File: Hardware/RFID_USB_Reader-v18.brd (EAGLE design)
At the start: 50.8 x 30.5 mm, 38 parts, among them Q1 MMBT2222, U1 ID-12/20SMD, U5 CH340C

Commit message: post checklist changes
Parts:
- added FRAME1: FRAME-LETTER, SparkFun-Aesthetics:CREATIVE_COMMONS
- added JP1, JP5: FIDUCIAL1X2, SparkFun:FIDUCIAL-1X2
- added LOGO4: REVISION, SparkFun-Aesthetics:REVISION
- added U$18: (no value), buzzard_labels (13):USB_RFID_READER0
- LED1: value GREEN -> BLUE
- U$17: device buzzard_labels (12):PWR0 -> buzzard_labels (13):USB_RFID_READER0
- U$2: value CREATIVE_COMMONS -> (none); device SparkFun:CREATIVE_COMMONS -> buzzard_labels (11):BZR3
- moved U$17 26.0 mm to (25.1, 12.7)
- moved U$2 15.1 mm to (0.25, 5.91)
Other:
- board text added: "A. England"
- board text added: "A. Weiss"
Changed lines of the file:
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@@
 <wire x1="0" y1="30.48" x2="0" y2="0" width="0.2032" layer="20"/>
 <text x="8.89" y="0.4445" size="1.27" layer="16" font="vector" ratio="15" rot="MR0">v13</text>
+<dimension x1="50.8" y1="30.48" x2="0" y2="30.48" x3="25.4" y3="36.83" textsize="1.778" layer="47" unit="inch"/>
+<dimension x1="0" y1="30.48" x2="0" y2="0" x3="-5.08" y3="15.24" textsize="1.778" layer="47" unit="inch"/>
+<dimension x1="2.54" y1="27.94" x2="48.26" y2="27.94" x3="25.4" y3="33.02" textsize="1.778" layer="47" unit="inch"/>
+<dimension x1="2.54" y1="27.94" x2="2.54" y2="2.54" x3="-1.27" y3="15.24" textsize="1.778" layer="47" unit="inch"/>
+<text x="26.67" y="-12.7" size="1.778" layer="51" font="vector">A. Weiss</text>
+<text x="26.67" y="-15.24" size="1.778" layer="51" font="vector">A. England</text>
 </plain>
 <attributes>
@@
 </autorouter>
 <elements>
-<element name="LED1" library="SparkFun-LED" package="LED-0603" value="GREEN" x="2.54" y="6.985" smashed="yes">
+<element name="LED1" library="SparkFun-LED" package="LED-0603" value="BLUE" x="2.54" y="6.985" smashed="yes">
 <attribute name="NAME" x="1.8415" y="6.096" size="0.4064" layer="25" rot="R90"/>
-<attribute name="PROD_ID" value="DIO-00821" x="2.54" y="6.985" size="1.778" layer="27" display="off"/>
-<attribute name="VALUE" value="GREEN" x="1.5875" y="6.477" size="0.4064" layer="27" rot="R90"/>
+<attribute name="PROD_ID" value="DIO-08575" x="2.54" y="6.985" size="1.778" layer="27" display="off"/>
+<attribute name="VALUE" value="BLUE" x="1.5875" y="6.477" size="0.4064" layer="27" rot="R90"/>
 </element>
 <element name="R1" library="SparkFun-Resistors" package="0603" value="330" x="5.08" y="7.9375" smashed="yes" rot="R270">
@@
 <attribute name="VALUE" x="10.795" y="10.922" size="0.6096" layer="27" ratio="10"/>
 </element>
-<element name="U$2" library="SparkFun" package="CREATIVE_COMMONS" value="CREATIVE_COMMONS" x="-2.54" y="-8.89"/>
 <element name="BUZZ" library="SparkFun-Jumpers" package="SMT-JUMPER_2_NO_NO-SILK" package3d_urn="urn:adsk.eagle:package:39277/1" value="buzz" x="12.7" y="6.35" rot="MR180"/>
 <element name="JP2" library="SparkFun" package="FIDUCIAL-1X2" value="FIDUCIAL1X2" x="6.35" y="5.08"/>
@@
 <element name="U$15" library="buzzard_labels (11)" package="TXR1" value="" x="49.2125" y="12.7" rot="MR0"/>
 <element name="U$16" library="buzzard_labels (11)" package="CP2" value="" x="49.2125" y="10.16" rot="MR0"/>
-<element name="U$17" library="buzzard_labels (12)" package="PWR0" value="" x="0.0635" y="5.588"/>
 <element name="LOGO1" library="SparkFun-Aesthetics" package="SFE_LOGO_NAME_FLAME_.1" value="SFE_LOGO_NAME_FLAME.1_INCH" x="31.75" y="15.24"/>
 <element name="LOGO2" library="SparkFun-Aesthetics" package="SFE_LOGO_NAME_FLAME_.1" value="SFE_LOGO_NAME_FLAME.1_INCH" x="22.86" y="15.24" rot="MR0"/>
 <element name="LOGO3" library="SparkFun-Aesthetics" package="OSHW-LOGO-S" value="OSHW-LOGOS" x="48.26" y="6.35" rot="MR0"/>
+<element name="FRAME1" library="SparkFun-Aesthetics" package="CREATIVE_COMMONS" value="FRAME-LETTER" x="-3.282121875" y="-12.7">
+<attribute name="DESIGNER" value="" x="-3.282121875" y="-12.7" size="1.778" layer="27" display="off"/>
+<attribute name="REV" value="" x="-3.282121875" y="-12.7" size="1.778" layer="27" display="off"/>
+</element>
+<element name="LOGO4" library="SparkFun-Aesthetics" package="REVISION" value="REVISION" x="8.89" y="-15.24"/>
+<element name="JP1" library="SparkFun" package="FIDUCIAL-1X2" value="FIDUCIAL1X2" x="39.37" y="26.67" rot="MR0"/>
+<element name="JP5" library="SparkFun" package="FIDUCIAL-1X2" value="FIDUCIAL1X2" x="6.35" y="5.08" rot="MR0"/>
+<element name="U$2" library="buzzard_labels (11)" package="BZR3" value="" x="0.254" y="5.9055"/>
+<element name="U$17" library="buzzard_labels (13)" package="USB_RFID_READER0" value="" x="25.0825" y="12.7"/>
+<element name="U$18" library="buzzard_labels (13)" package="USB_RFID_READER0" value="" x="29.591" y="12.7" rot="MR0"/>
 </elements>
 <signals>

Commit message: post review changes
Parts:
- removed J2: (no value), SparkFun-Connectors:1X05_NO_SILK
- removed U$2: (no value), buzzard_labels (11):BZR3
- added J1: (no value), SparkFun-Connectors:1X07
- added U$19: (no value), buzzard_labels (14):ANT11
- added U$20: (no value), buzzard_labels (14):ANT13
- added U$21: (no value), buzzard_labels (14):ANT22
- added U$22: (no value), buzzard_labels (15):ANT24
- added U$23: (no value), buzzard_labels (15):IND0
- moved U$10 2.54 mm to (44.4, 15.2)
- moved U$14 2.54 mm to (49.1, 17.8)
- moved U$15 2.54 mm to (49.2, 15.2)
- moved U$9 2.54 mm to (45.3, 17.8)
- moved U$1 2.54 mm to (45.5, 7.62)
- moved U$16 2.54 mm to (49.2, 7.62)
- moved U$11 2.54 mm to (44.4, 22.9)
- moved U$12 2.54 mm to (49.1, 22.9)
- moved U$13 2.54 mm to (49.1, 20.3)
- moved U$3 2.54 mm to (44.6, 20.3)
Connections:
- net LED renamed INDICATOR
- new net ANT1: J1.3, U1.3
- new net ANT2: J1.2, U1.4
- net CP: now also J1.1; no longer J2.1
- net GND: now also J1.6; no longer J2.4
- net TX-O: now also J1.5; no longer J2.3
- net TX-O-RS232: now also J1.4; no longer J2.2
- net VCC: now also J1.7; no longer J2.5
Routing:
- net ANT1: track 0.00 -> 23.6 mm, vias 0 -> 1
- net ANT2: track 0.00 -> 21.9 mm, vias 0 -> 1
- net TX-O-RS232: track 37.7 -> 35.1 mm
- net TX-O: track 59.5 -> 57.0 mm
- net N$4: track 6.81 -> 5.39 mm
- net VCC: track 122.1 -> 121.1 mm
- net CP: track 25.3 -> 24.5 mm
- net GND: vias 7 -> 8

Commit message: post QC checklist changes
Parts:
- moved LOGO3 6.35 mm to (43.2, 2.54)
- moved JP2 1.27 mm to (5.08, 5.08)
- moved JP5 1.27 mm to (5.08, 5.08)
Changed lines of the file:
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@@
 </element>
 <element name="BUZZ" library="SparkFun-Jumpers" package="SMT-JUMPER_2_NO_NO-SILK" package3d_urn="urn:adsk.eagle:package:39277/1" value="buzz" x="12.7" y="6.35" rot="MR180"/>
-<element name="JP2" library="SparkFun" package="FIDUCIAL-1X2" value="FIDUCIAL1X2" x="6.35" y="5.08"/>
+<element name="JP2" library="SparkFun" package="FIDUCIAL-1X2" value="FIDUCIAL1X2" x="5.08" y="5.08"/>
 <element name="JP3" library="SparkFun" package="FIDUCIAL-1X2" value="FIDUCIAL1X2" x="39.37" y="26.67"/>
 <element name="U5" library="SparkFun-IC-Comms" package="SO016" value="CH340C" x="12.7" y="20.32" rot="R270">
@@
 <element name="LOGO1" library="SparkFun-Aesthetics" package="SFE_LOGO_NAME_FLAME_.1" value="SFE_LOGO_NAME_FLAME.1_INCH" x="31.75" y="15.24"/>
 <element name="LOGO2" library="SparkFun-Aesthetics" package="SFE_LOGO_NAME_FLAME_.1" value="SFE_LOGO_NAME_FLAME.1_INCH" x="22.86" y="15.24" rot="MR0"/>
-<element name="LOGO3" library="SparkFun-Aesthetics" package="OSHW-LOGO-S" value="OSHW-LOGOS" x="48.26" y="6.35" rot="MR0"/>
+<element name="LOGO3" library="SparkFun-Aesthetics" package="OSHW-LOGO-S" value="OSHW-LOGOS" x="43.18" y="2.54" rot="MR0"/>
 <element name="FRAME1" library="SparkFun-Aesthetics" package="CREATIVE_COMMONS" value="FRAME-LETTER" x="-3.282121875" y="-12.7">
 <attribute name="DESIGNER" value="" x="-3.282121875" y="-12.7" size="1.778" layer="27" display="off"/>
@@
 <element name="LOGO4" library="SparkFun-Aesthetics" package="REVISION" value="REVISION" x="8.89" y="-15.24"/>
 <element name="JP1" library="SparkFun" package="FIDUCIAL-1X2" value="FIDUCIAL1X2" x="39.37" y="26.67" rot="MR0"/>
-<element name="JP5" library="SparkFun" package="FIDUCIAL-1X2" value="FIDUCIAL1X2" x="6.35" y="5.08" rot="MR0"/>
+<element name="JP5" library="SparkFun" package="FIDUCIAL-1X2" value="FIDUCIAL1X2" x="5.08" y="5.08" rot="MR0"/>
 <element name="U$17" library="buzzard_labels (13)" package="USB_RFID_READER0" value="" x="25.0825" y="12.7"/>
 <element name="U$18" library="buzzard_labels (13)" package="USB_RFID_READER0" value="" x="29.591" y="12.7" rot="MR0"/>

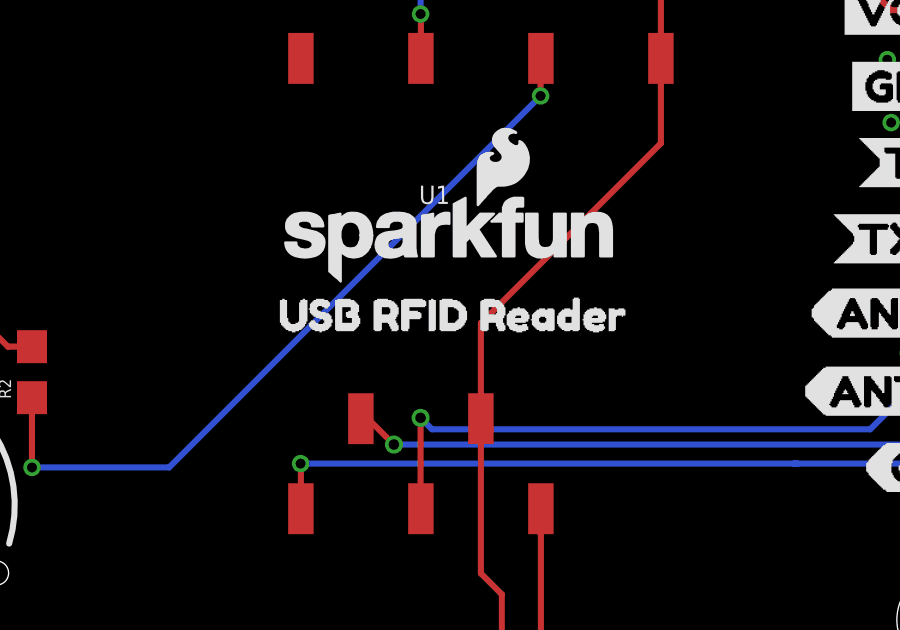
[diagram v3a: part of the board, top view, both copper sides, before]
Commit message: changing name to USB-C
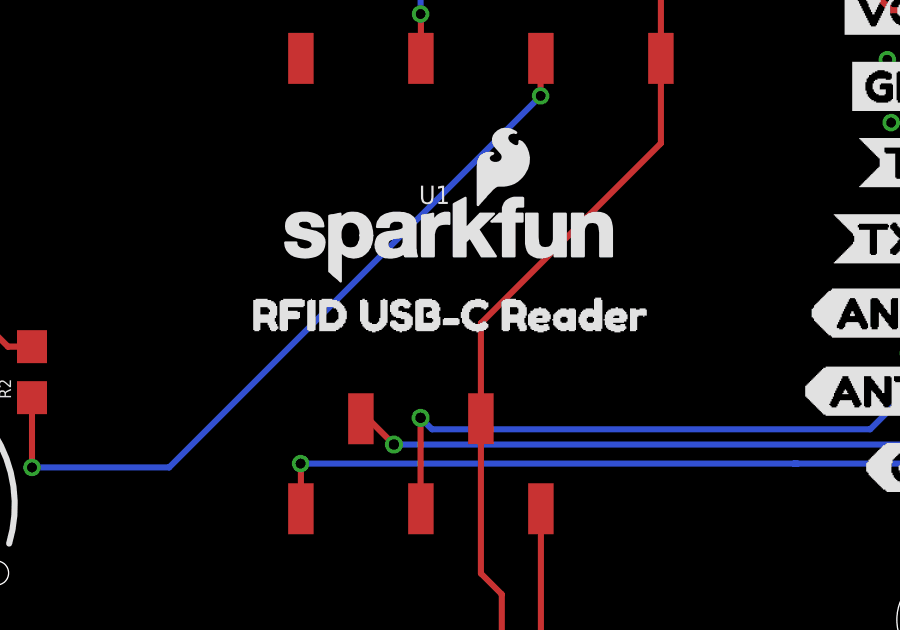
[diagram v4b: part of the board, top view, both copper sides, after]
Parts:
- U$17, U$18: device buzzard_labels (13):USB_RFID_READER0 -> buzzard_labels (16):RFID_USB#C_READER0
- moved U$17 0.89 mm to (24.2, 12.7)
- moved U$18 0.76 mm to (30.4, 12.7)
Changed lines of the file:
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@@
 <element name="JP1" library="SparkFun" package="FIDUCIAL-1X2" value="FIDUCIAL1X2" x="39.37" y="26.67" rot="MR0"/>
 <element name="JP5" library="SparkFun" package="FIDUCIAL-1X2" value="FIDUCIAL1X2" x="5.08" y="5.08" rot="MR0"/>
-<element name="U$17" library="buzzard_labels (13)" package="USB_RFID_READER0" value="" x="25.0825" y="12.7"/>
-<element name="U$18" library="buzzard_labels (13)" package="USB_RFID_READER0" value="" x="29.591" y="12.7" rot="MR0"/>
+<element name="U$17" library="buzzard_labels (16)" package="RFID_USB#C_READER0" value="" x="24.1935" y="12.7"/>
+<element name="U$18" library="buzzard_labels (16)" package="RFID_USB#C_READER0" value="" x="30.353" y="12.7" rot="MR0"/>
 <element name="J1" library="SparkFun-Connectors" package="1X07" value="" x="49.53" y="7.62" rot="R90"/>
 <element name="U$19" library="buzzard_labels (14)" package="ANT11" value="" x="43.688" y="12.7635"/>

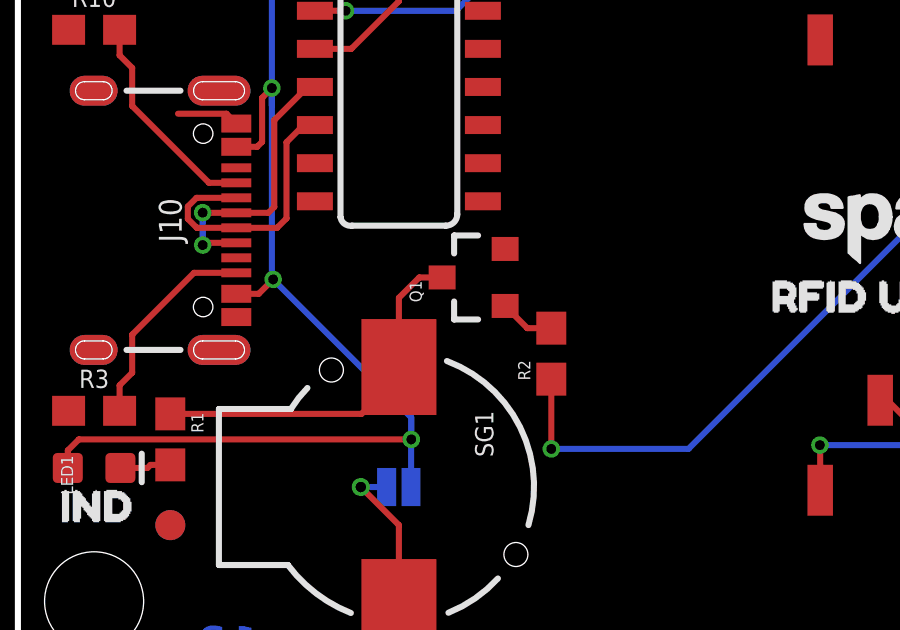
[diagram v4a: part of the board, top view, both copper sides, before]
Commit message: updating Buzzer and npn transistor to have PROD_ID
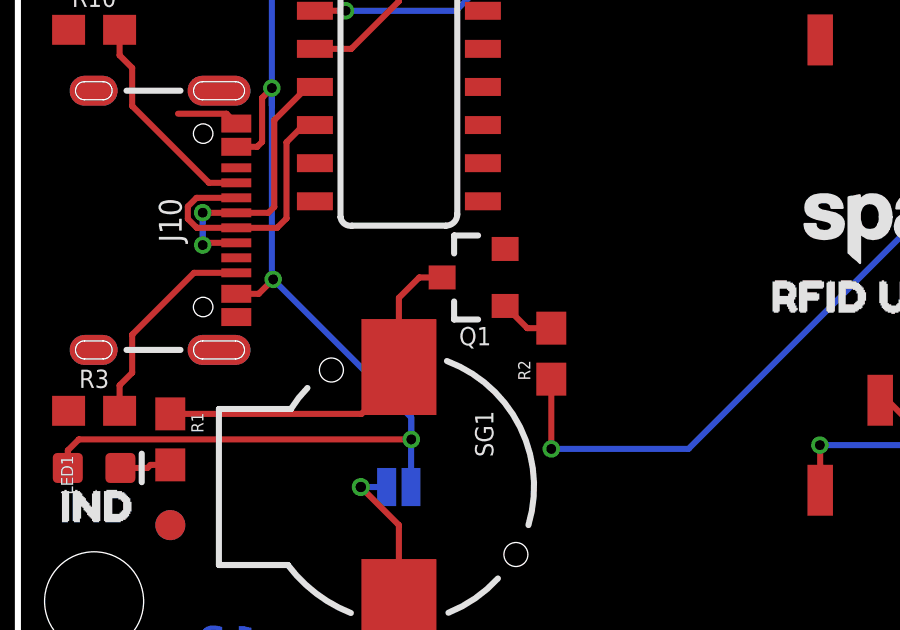
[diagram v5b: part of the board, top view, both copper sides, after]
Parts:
- Q1: value MMBT2222 -> 600mA/40V; device SparkFun:SOT23-3 -> SparkFun-DiscreteSemi:SOT23-3
- SG1: value BUZZERSMD2 -> BUZZER-SMD; device SparkFun:BUZZER-CCV -> SparkFun-Electromechanical:BUZZER-CCV
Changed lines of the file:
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@@
 <element name="U$6" library="SparkFun" package="STAND-OFF" value="STAND-OFF" x="48.26" y="27.94"/>
 <element name="U$7" library="SparkFun" package="STAND-OFF" value="STAND-OFF" x="48.26" y="2.54"/>
-<element name="Q1" library="SparkFun" package="SOT23-3" value="MMBT2222" x="15.24" y="13.335" rot="R90"/>
+<element name="Q1" library="SparkFun-DiscreteSemi" package="SOT23-3" value="600mA/40V" x="15.24" y="13.335" rot="R90">
+<attribute name="PROD_ID" value="TRANS-08049" x="15.24" y="13.335" size="1.778" layer="27" rot="R90" display="off"/>
+<attribute name="VALUE" value="600mA/40V" x="15.24" y="13.335" size="1.778" layer="27" rot="R90" display="off"/>
+</element>
 <element name="R2" library="SparkFun-Resistors" package="0603" value="180" x="17.78" y="10.795" smashed="yes" rot="R90">
 <attribute name="NAME" x="17.0815" y="9.906" size="0.4064" layer="25" rot="R90"/>
@@
 <attribute name="VALUE" value="180" x="17.0815" y="10.922" size="0.4064" layer="27" rot="R180"/>
 </element>
-<element name="SG1" library="SparkFun" package="BUZZER-CCV" value="BUZZERSMD2" x="12.7" y="6.35" smashed="yes" rot="R270">
+<element name="SG1" library="SparkFun-Electromechanical" package="BUZZER-CCV" value="BUZZER-SMD" x="12.7" y="6.35" smashed="yes" rot="R270">
 <attribute name="NAME" x="15.24" y="8.89" size="0.6096" layer="25" ratio="10" rot="R270"/>
+<attribute name="PROD_ID" value="COMP-08568" x="12.7" y="6.35" size="1.778" layer="27" rot="R270" display="off"/>
 <attribute name="VALUE" x="10.795" y="10.922" size="0.6096" layer="27" ratio="10"/>
 </element>
